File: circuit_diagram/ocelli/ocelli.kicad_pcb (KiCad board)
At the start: 2 copper layers, 80 x 58 mm, 114 parts, among them J1 Conn_01x06, J2 Conn_01x06, J3 Conn_01x06, J4 Conn_01x06, J5 Conn_01x08, J6 Conn_01x02, J7 Conn_01x02, Q1 BSS138, Q10 BSS138, Q2 ST-1KL3A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

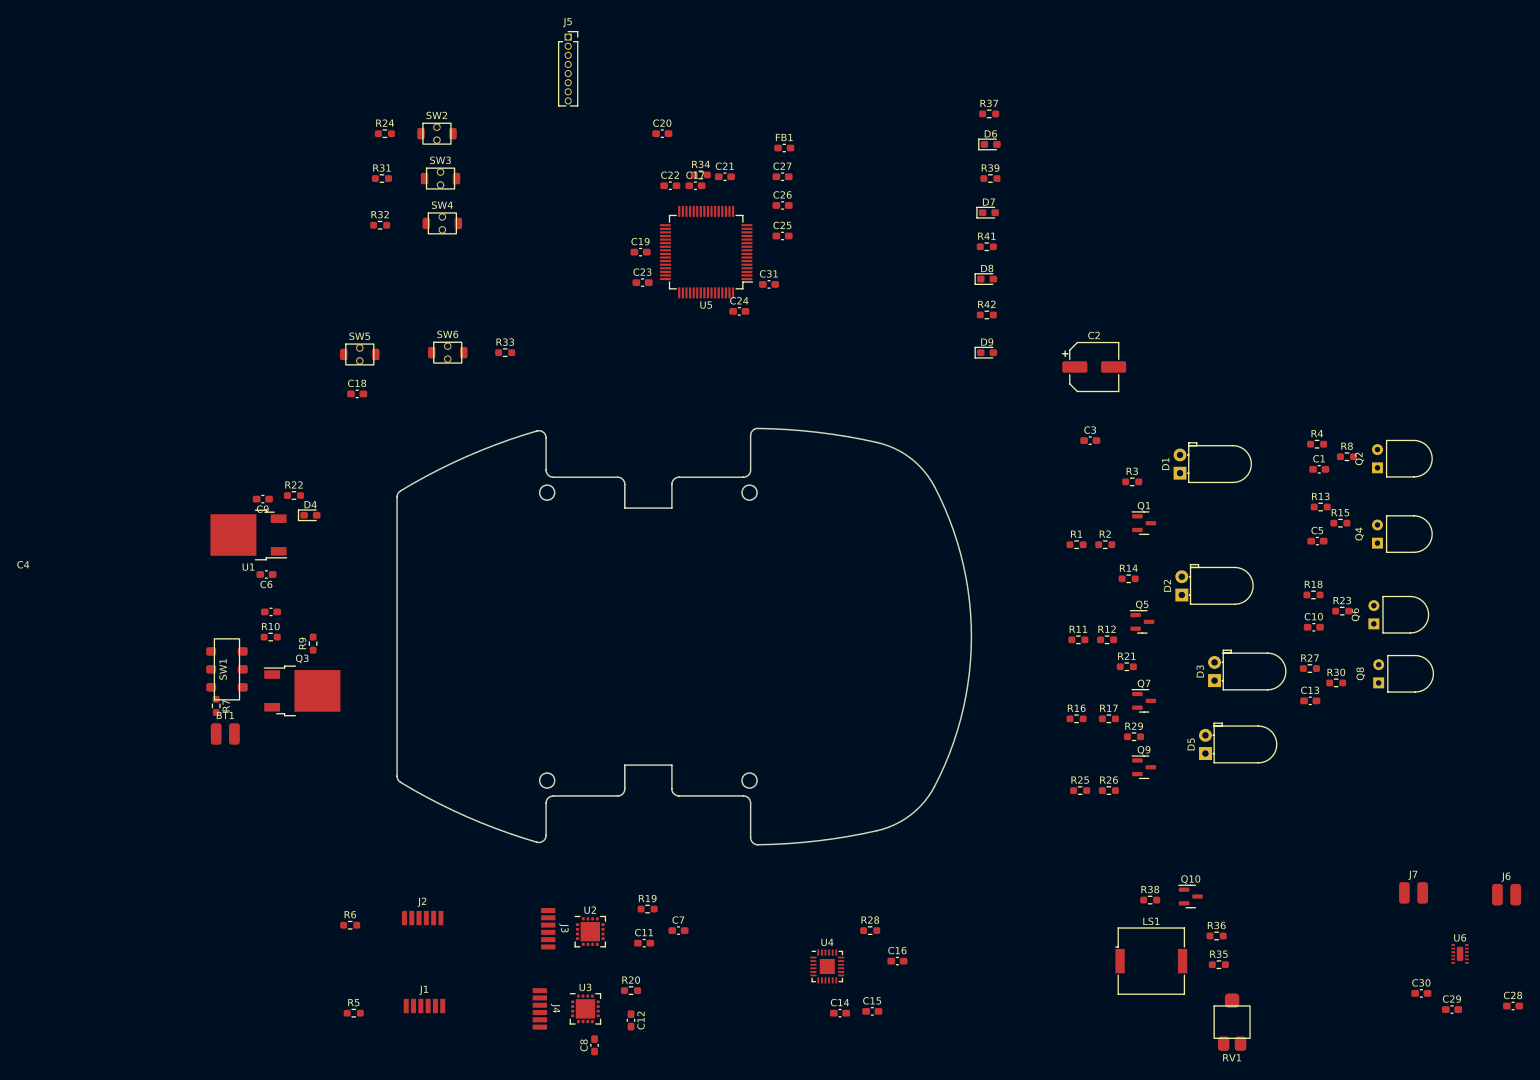
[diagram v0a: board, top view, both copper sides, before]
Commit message: モータ位置変更
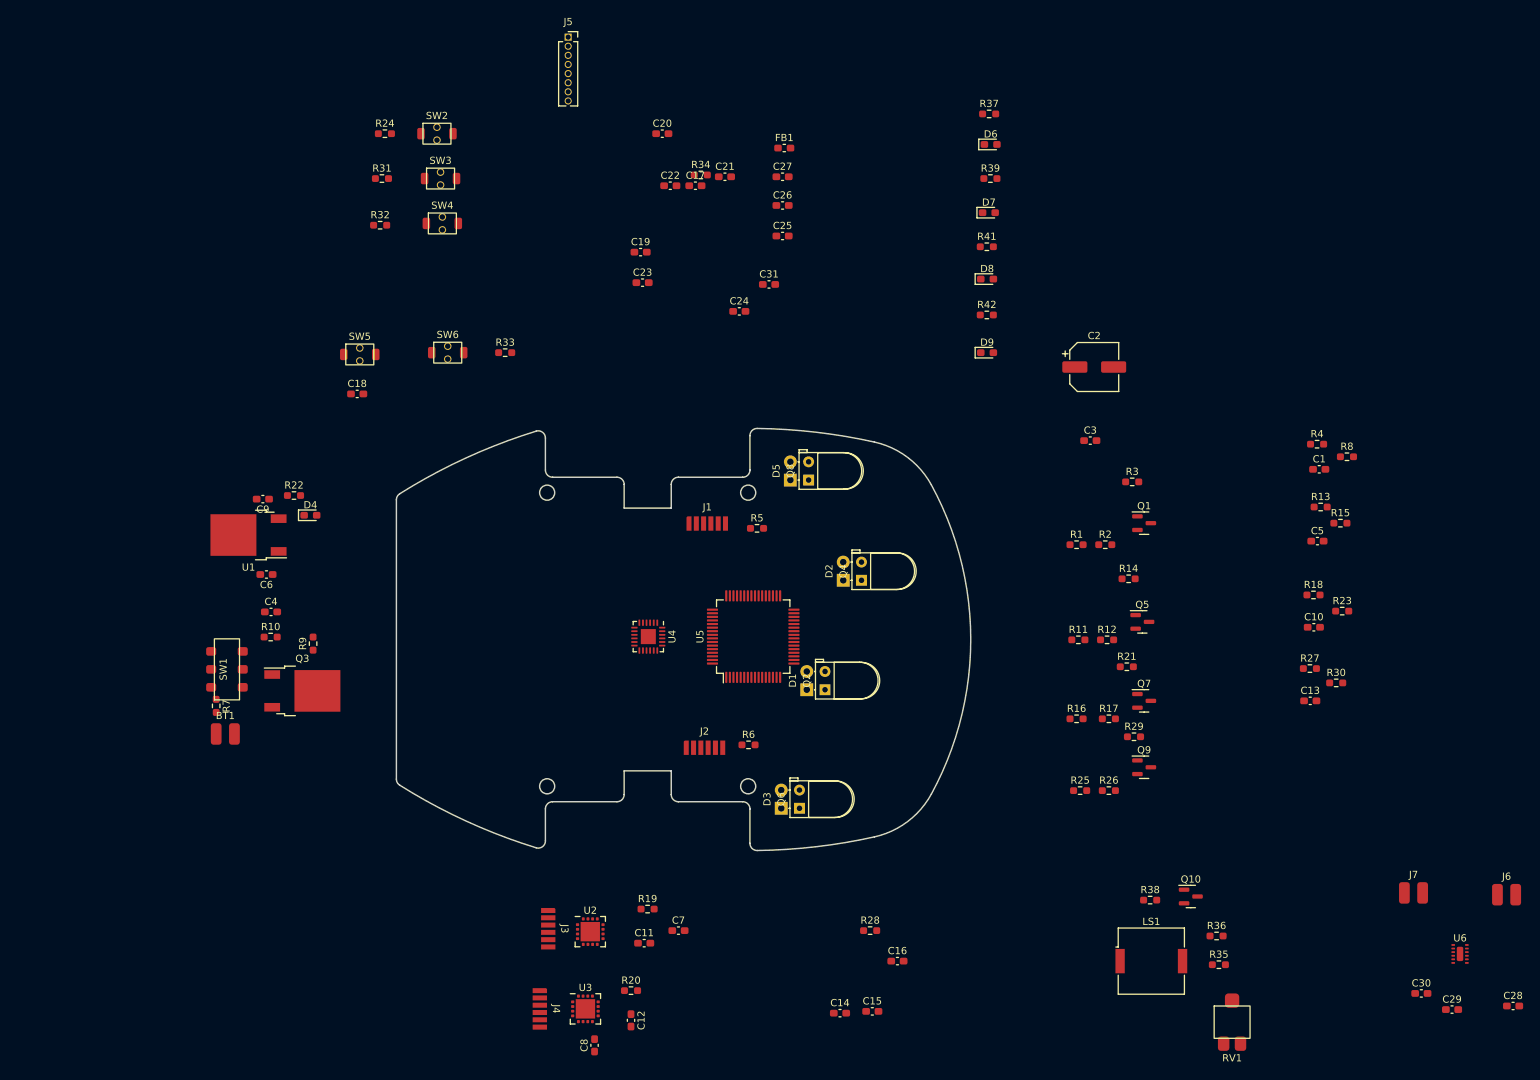
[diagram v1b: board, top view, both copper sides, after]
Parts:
- moved R5 87.8 mm to (162.3, 85.5)
- moved Q8 84.3 mm to (169.5, 78.7)
- moved Q6 84.0 mm to (168.2, 124.5)
- moved Q2 82.9 mm to (171.8, 108.0)
- moved J1 77.9 mm to (155.4, 84.8)
- moved Q4 72.1 mm to (176.9, 92.7)
- moved D5 69.2 mm to (167.0, 78.7)
- moved D3 62.9 mm to (165.7, 124.5)
- moved R6 60.9 mm to (161.1, 115.6)
- moved D1 60.1 mm to (169.3, 107.9)
- moved U5 53.9 mm to (161.8, 100.5), turned to 90 degrees
- moved U4 52.3 mm to (147.2, 100.5), turned to -90 degrees
- moved D2 47.2 mm to (174.3, 92.7)
- moved J2 45.9 mm to (155.0, 116.0)
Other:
- board size 80 x 58 mm -> 80 x 58.8 mm

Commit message: 部品配置中
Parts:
- U2, U3: moved to B.Cu
- moved J6 125.9 mm to (149.3, 91.1)
- moved C28 125.7 mm to (157.1, 92.2)
- moved U6 120.2 mm to (153.1, 90.3), turned to -90 degrees
- moved C29 120.0 mm to (157.1, 89.4)
- moved C30 116.6 mm to (152.7, 94.1)
- moved J7 110.2 mm to (151.0, 96.6)
- moved RV1 104.4 mm to (132.0, 114.4), turned to 90 degrees
- moved R35 103.7 mm to (129.7, 109.5), turned to -90 degrees
- moved R36 100.2 mm to (131.6, 109.5), turned to -90 degrees
- moved J5 95.0 mm to (112.3, 109.0)
- moved LS1 94.7 mm to (132.9, 102.6)
- moved Q10 91.1 mm to (135.8, 109.5)
- moved R37 84.1 mm to (137.3, 89.2), turned to 180 degrees
- moved D6 83.6 mm to (133.9, 89.2)
- moved R38 83.5 mm to (138.8, 108.3), turned to 90 degrees
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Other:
- outline, holes or cut-outs redrawn

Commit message: 一通りパターンを繋いだ
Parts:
- added R: MountingHole_2.2mm_M2, MountingHole:MountingHole_2.2mm_M2, F.Cu at (130.0, 80.0)
- added REF**: MountingHole_2.2mm_M2, MountingHole:MountingHole_2.2mm_M2, F.Cu at (158.0, 120.9)
- added REF**: MountingHole_2.2mm_M2, MountingHole:MountingHole_2.2mm_M2, F.Cu at (158.0, 80.0)
- added REF**: MountingHole_2.2mm_M2, MountingHole:MountingHole_2.2mm_M2, F.Cu at (130.0, 120.9)
- moved R24 79.5 mm to (164.6, 88.7), turned to 90 degrees
- moved FB1 77.5 mm to (164.8, 110.0), turned to 90 degrees
- moved R31 77.5 mm to (167.6, 88.7), turned to 90 degrees
- moved R8 77.3 mm to (175.6, 110.6)
- moved C8 76.5 mm to (102.8, 90.5), turned to 0 degrees
- moved R32 75.9 mm to (170.6, 88.7), turned to 90 degrees
- moved C1 74.8 mm to (173.2, 109.7), turned to -90 degrees
- moved C12 74.6 mm to (102.8, 92.3), turned to 180 degrees
- moved C20 74.5 mm to (151.3, 105.0), turned to -90 degrees
- moved R4 73.6 mm to (175.6, 108.8)
- moved C27 73.5 mm to (167.8, 110.0), turned to -90 degrees
- moved SW2 71.1 mm to (164.6, 84.0), turned to 90 degrees
- moved R20 70.6 mm to (105.2, 91.4), turned to -90 degrees
- moved U3 70.6 mm to (102.8, 91.5), turned to 90 degrees
- moved R30 69.8 mm to (175.6, 88.8)
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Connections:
- U5 pad 24: RIGHT_SIDE_AD -> RIGHT_FRONT_AD
- U5 pad 25: RIGHT_FRONT_AD -> RIGHT_SIDE_AD
- U5 pad 26: LEFT_FRONT_AD -> LEFT_SIDE_AD
- U5 pad 27: LEFT_SIDE_AD -> LEFT_FRONT_AD
- U5 pad 41: PWM_L -> DIR_L
- U5 pad 42: PWM_R -> PWM_L
- U5 pad 43: DIR_L -> DIR_R
- U5 pad 44: DIR_R -> PWM_R
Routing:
- net +3.3V: track 0.00 -> 405.5 mm, vias 0 -> 2
- net +3.3VA: track 0.00 -> 101.9 mm, vias 0 -> 1
- net GND: track 0.00 -> 76.9 mm, vias 0 -> 23
- net +BATT: track 0.00 -> 63.6 mm
- net UART_RX: track 0.00 -> 58.7 mm, vias 0 -> 1
- net SPI2_SCLK: track 0.00 -> 58.3 mm, vias 0 -> 3
- net NRST: track 0.00 -> 57.1 mm
- net SWCLK: track 0.00 -> 56.6 mm, vias 0 -> 1
- net SWDIO: track 0.00 -> 55.6 mm, vias 0 -> 1
- net SPI2_MOSI: track 0.00 -> 55.0 mm, vias 0 -> 2
- net VBAT_AD: track 0.00 -> 54.2 mm, vias 0 -> 4
- net SPI2_MISO: track 0.00 -> 51.3 mm, vias 0 -> 2
- net SWO: track 0.00 -> 49.7 mm, vias 0 -> 1
- net UART_TX: track 0.00 -> 49.1 mm, vias 0 -> 2
- net BUZZER: track 0.00 -> 35.4 mm, vias 0 -> 2
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- added copper zone on B.Cu, net GND
- added copper zone on F.Cu, net GND
- added copper zone on B.Cu, net GND_L
- added copper zone on F.Cu, net GND_L
- added copper zone on B.Cu, net GND_R
- added copper zone on F.Cu, net GND_R
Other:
- board size 80 x 58.8 mm -> 89.5 x 58.8 mm

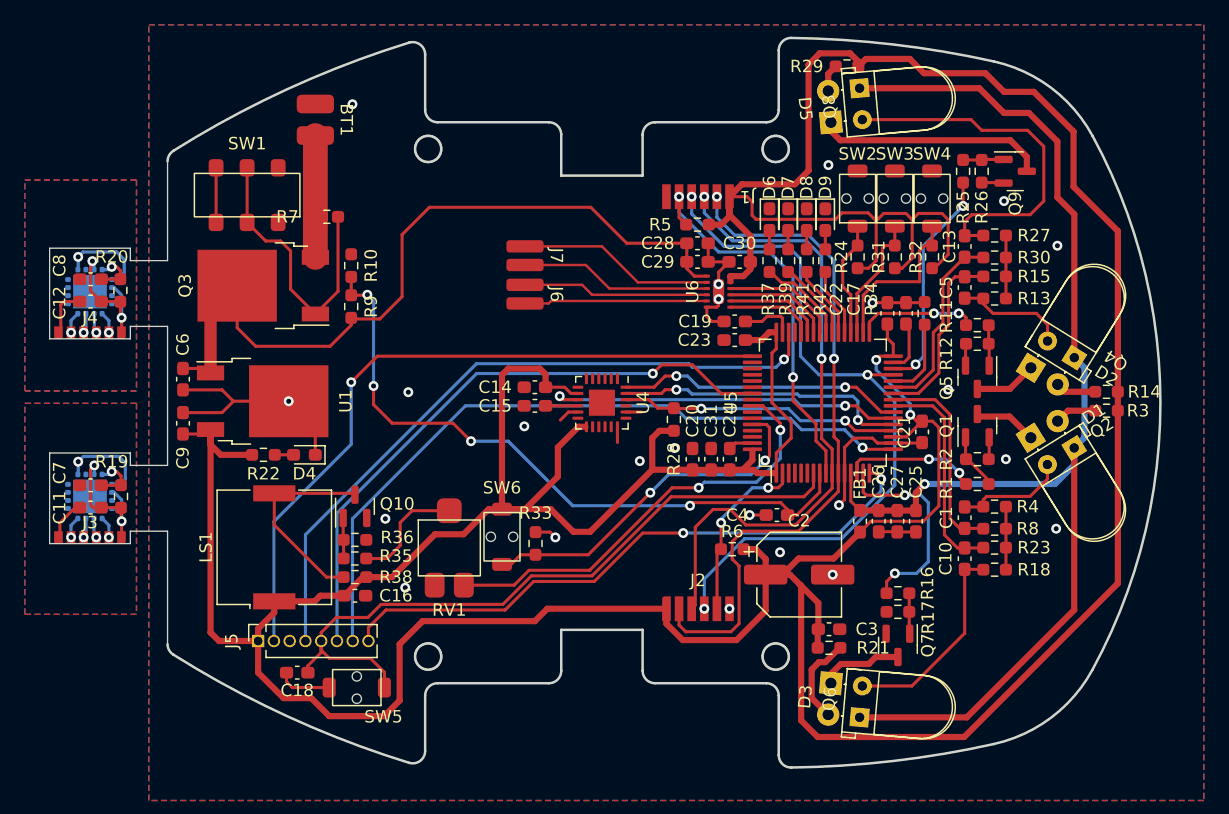
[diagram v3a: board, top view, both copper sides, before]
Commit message: 対処すべきDRCエラーに対処した
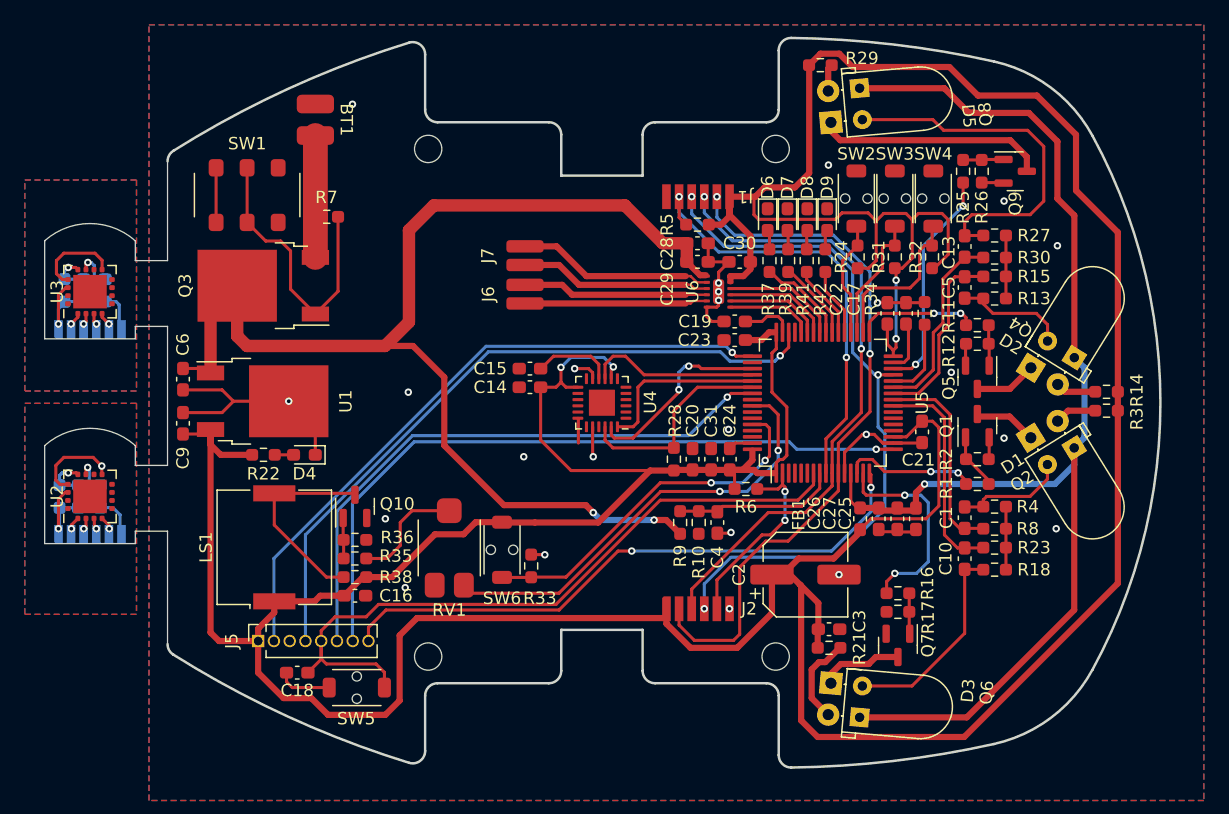
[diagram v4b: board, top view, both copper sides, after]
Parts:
- C11, C12, C7, C8, J3, J4, R19, R20: moved to B.Cu
- U2, U3: moved to F.Cu
- moved R10 34.8 mm to (151.8, 110.1), turned to -90 degrees
- moved R9 31.7 mm to (150.3, 110.1)
- moved R6 4.97 mm to (155.6, 107.4), turned to 180 degrees
- moved R19 4.95 mm to (100.3, 108.0)
- moved C4 4.84 mm to (153.3, 110.1), turned to -90 degrees
- moved R20 4.50 mm to (100.7, 91.4)
- moved R28 3.20 mm to (149.8, 105.0)
- moved C15 3.03 mm to (138.2, 97.7)
- moved R29 2.15 mm to (161.6, 73.2), turned to 0 degrees
- moved R33 1.85 mm to (138.3, 113.6)
- moved SW6 1.05 mm to (135.9, 112.3)
- moved C2 0.51 mm to (160.4, 114.3)
- moved C14 0.40 mm to (138.2, 99.2)
- moved C12 0.30 mm to (103.1, 92.3), turned to 0 degrees
- moved C8 0.30 mm to (103.1, 90.5), turned to 180 degrees
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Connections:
- U5 pad 20: SPI1_CS -> unconnected-(U5-Pad20)
- U5 pad 21: SPI1_SCLK -> unconnected-(U5-Pad21)
- U5 pad 22: SPI1_MISO -> unconnected-(U5-Pad22)
- U5 pad 23: SPI1_MOSI -> unconnected-(U5-Pad23)
- U5 pad 51: unconnected-(U5-Pad51) -> SPI1_SCLK
- U5 pad 52: unconnected-(U5-Pad52) -> SPI1_MISO
- U5 pad 53: unconnected-(U5-Pad53) -> SPI1_MOSI
- U5 pad 54: unconnected-(U5-Pad54) -> SPI1_CS
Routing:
- net VBAT_AD: track 54.2 -> 13.3 mm, vias 4 -> 0
- net +BATT: track 63.6 -> 97.9 mm, vias 0 -> 2
- net SPI1_MISO: track 29.2 -> 13.9 mm, vias 2 -> 0
- net +3.3V: track 405.5 -> 393.7 mm, vias 2 -> 4
- net SPI1_MOSI: track 23.1 -> 14.0 mm, vias 2 -> 0
- net SPI1_SCLK: track 23.7 -> 15.6 mm
- net SPI1_CS: track 22.6 -> 17.0 mm, vias 2 -> 0
- net SPI2_CS0: track 32.1 -> 36.1 mm
- net SWCLK: track 56.6 -> 52.6 mm
- net Net-(C15-Pad1): track 2.60 -> 6.53 mm
- net SPI2_MOSI: track 55.0 -> 57.4 mm
- net SWO: track 49.7 -> 47.9 mm
- net SPI2_CS1: track 14.1 -> 15.9 mm
- net GND: track 76.9 -> 75.2 mm, vias 23 -> 24
- net UART_RX: track 58.7 -> 57.0 mm
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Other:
- board size 89.5 x 58.8 mm -> 89.9 x 58.8 mm

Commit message: 適当にビアを打ってみた
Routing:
- net GND: track 75.2 -> 78.9 mm, vias 24 -> 59
- net +3.3VA: track 102.0 -> 101.0 mm
- net SPI2_MISO: track 50.5 -> 51.1 mm
- net GND_R: vias 0 -> 1
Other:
- outline, holes or cut-outs redrawn

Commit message: アイコンシルク追加
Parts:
- added G***: LOGO, ocelli_lib:kuwamai_icon, F.Cu at (177.1, 120.4)
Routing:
- net GND: track 78.9 -> 78.5 mm, vias 59 -> 60
- net SPI2_SCLK: vias 3 -> 4
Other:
- board text added: "ocelli v1.0 Kuwamai"

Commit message: フットプリント修正
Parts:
- U4: footprint Package_DFN_QFN:HVQFN-24-1EP_4x4mm_P0.5mm_EP2.1x2.1mm -> Package_DFN_QFN:QFN-24-1EP_3x3mm_P0.4mm_EP1.75x1.6mm_ThermalVias

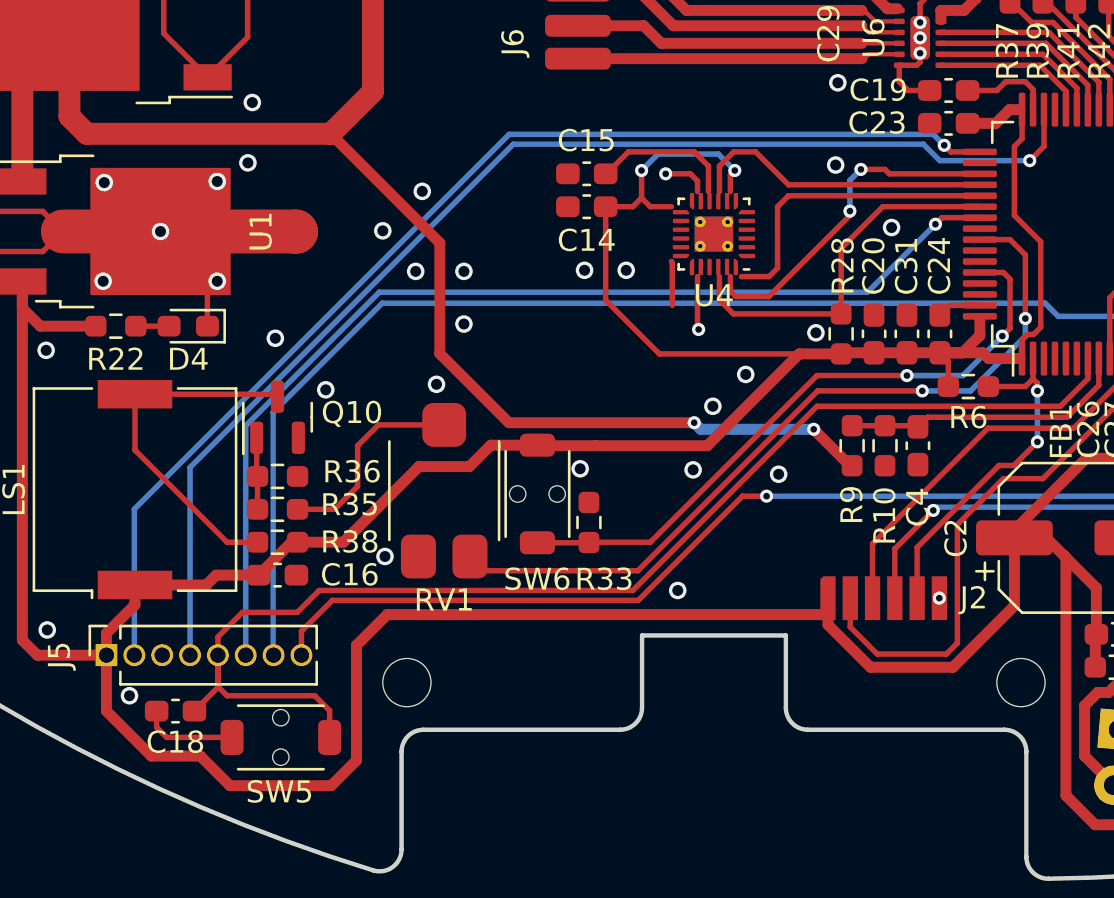
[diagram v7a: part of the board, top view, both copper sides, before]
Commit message: フットプリント修正
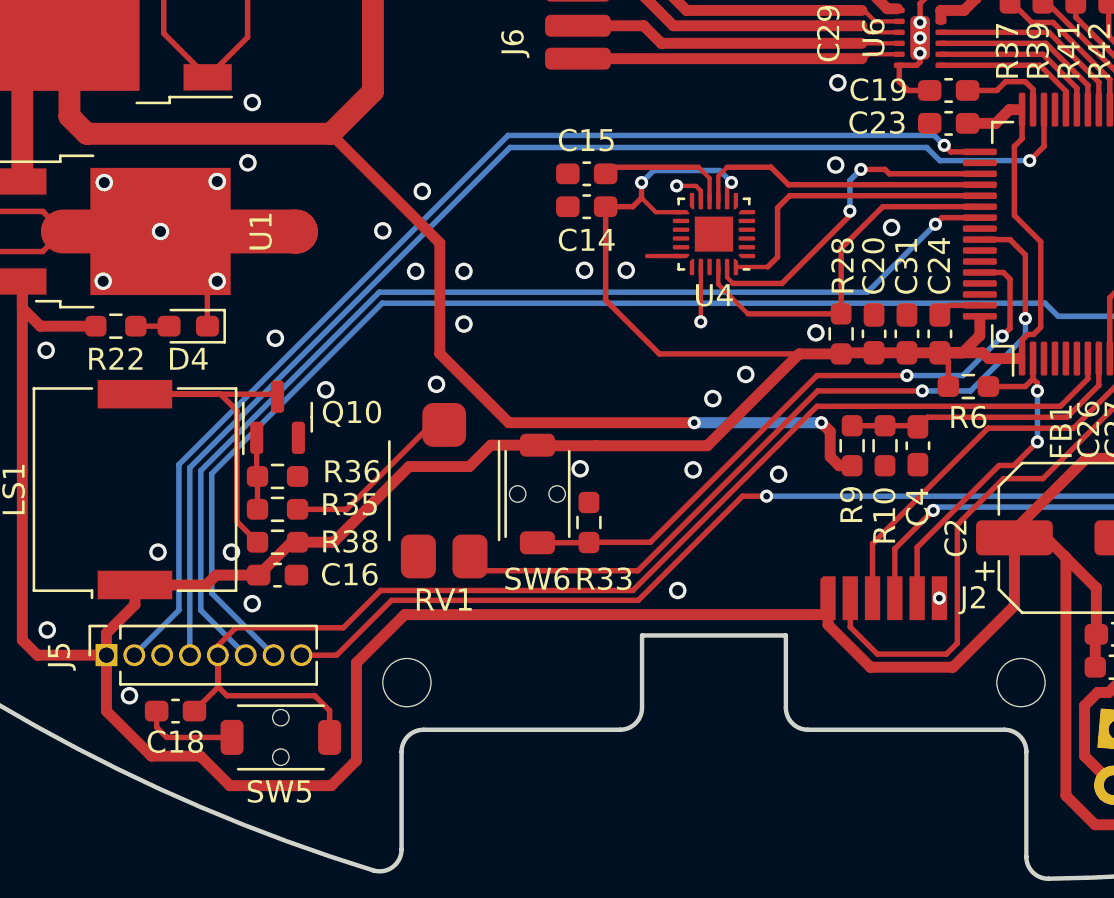
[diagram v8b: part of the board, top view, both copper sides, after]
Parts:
- U4: footprint Package_DFN_QFN:QFN-24-1EP_3x3mm_P0.4mm_EP1.75x1.6mm_ThermalVias -> Package_DFN_QFN:QFN-24-1EP_3x3mm_P0.4mm_EP1.75x1.6mm
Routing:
- net UART_RX: track 57.0 -> 59.3 mm
- net SWO: track 47.9 -> 49.6 mm
- net Net-(LS1-Pad2): track 16.4 -> 17.9 mm
- net Net-(R35-Pad2): track 9.37 -> 8.28 mm
- net +3.3V: track 393.8 -> 392.9 mm
- net GND: track 78.5 -> 77.7 mm, vias 60 -> 62
- net +BATT: track 97.7 -> 98.4 mm
- net UART_TX: track 48.6 -> 48.0 mm
